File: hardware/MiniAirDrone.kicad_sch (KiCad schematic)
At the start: 15 parts, among them J1 USB_C_Receptacle_USB2.0, Q1 UMH3N, U1 CH340C, U2 ESP32-WROOM-32

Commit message: mpu6050
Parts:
- added C5: 0.1uF, symbol Device:C
- added C6: 2.2nF, symbol Device:C
- added R4, R? (x2): 10K, symbol Device:R
- added U3: MPU-6050, Sensor_Motion:InvenSense_QFN-24_4x4mm_P0.5mm, symbol Sensor_Motion:MPU-6050
- added U?: TS1117BCW33_RPG, Package_TO_SOT_SMD:SOT-223-3_TabPin2, symbol Regulator_Linear:TS1117BCW33_RPG
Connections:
- net +3.3V: now also R4.1, R?.1, R?.1, U3.13 (VDD), U3.8 (VDDIO), U?.2 (Output)
- net +5V: now also U?.3 (Input)
- net GND: now also C5.2, C6.2, U3.1 (CLKIN), U3.11 (FSYNC), U3.18 (GND), U3.9 (AD0), U?.1 (GND)
- new net: C5.1, U3.10 (REGOUT)
- new net: C6.1, U3.20 (CPOUT)
- new net AUX_SCL: R?.2, U3.7 (AUX_SCL)
- new net AUX_SDA: R?.2, U3.6 (AUX_SDA)
- new net IIC0_SCL: U3.23 (SCL)
- new net IIC0_SDA: U3.24 (SDA)
- new net MPU_INT: R4.2, U3.12 (INT)
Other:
- note added: "MPU6050"
- note added: "POWER"
- moved on the sheet: C1, C2, J1, Q1A, Q1B, R1, R2, R3, TP1, TP2, U1

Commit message: sth
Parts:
- removed R4, R? (x2): 10K, symbol Device:R
- added U?: MS5611-01BA, Package_LGA:LGA-8_3x5mm_P1.25mm, symbol Sensor_Pressure:MS5611-01BA
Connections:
- net +3.3V: now also U?.1 (VDD), U?.2 (PS)
- net GND: now also U?.3 (GND), U?.4 (CSB), U?.5 (CSB)
- net IIC0_SCL: now also U2.36 (IO22), U?.8 (SCLK)
- net IIC0_SDA: now also U?.7 (SDI/SDA)
- net AUX_SCL: no longer names the net of U3.7 (AUX_SCL)
- net AUX_SDA: no longer names the net of U3.6 (AUX_SDA)
- net MPU_INT: no longer names the net of U3.12 (INT)
- no-connect marks 7 -> 11
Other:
- note added: "IIC0_SDA"
- note added: "MS5611 气压计"

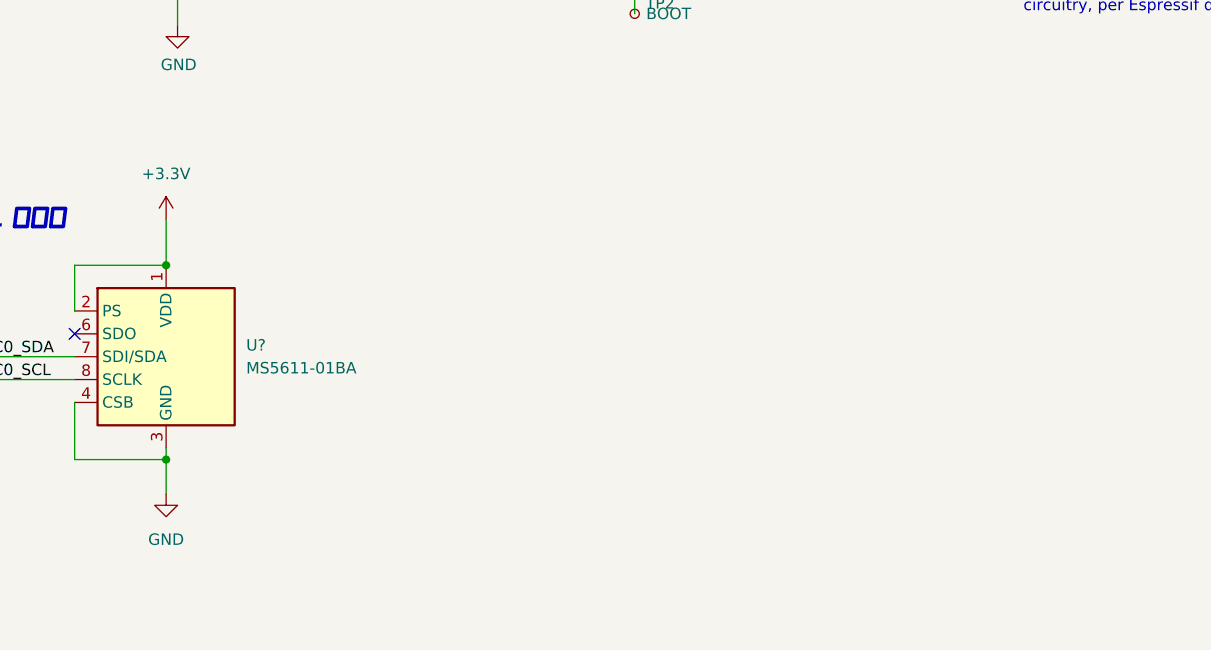
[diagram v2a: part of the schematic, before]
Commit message: Update MiniAirDrone.kicad_sch
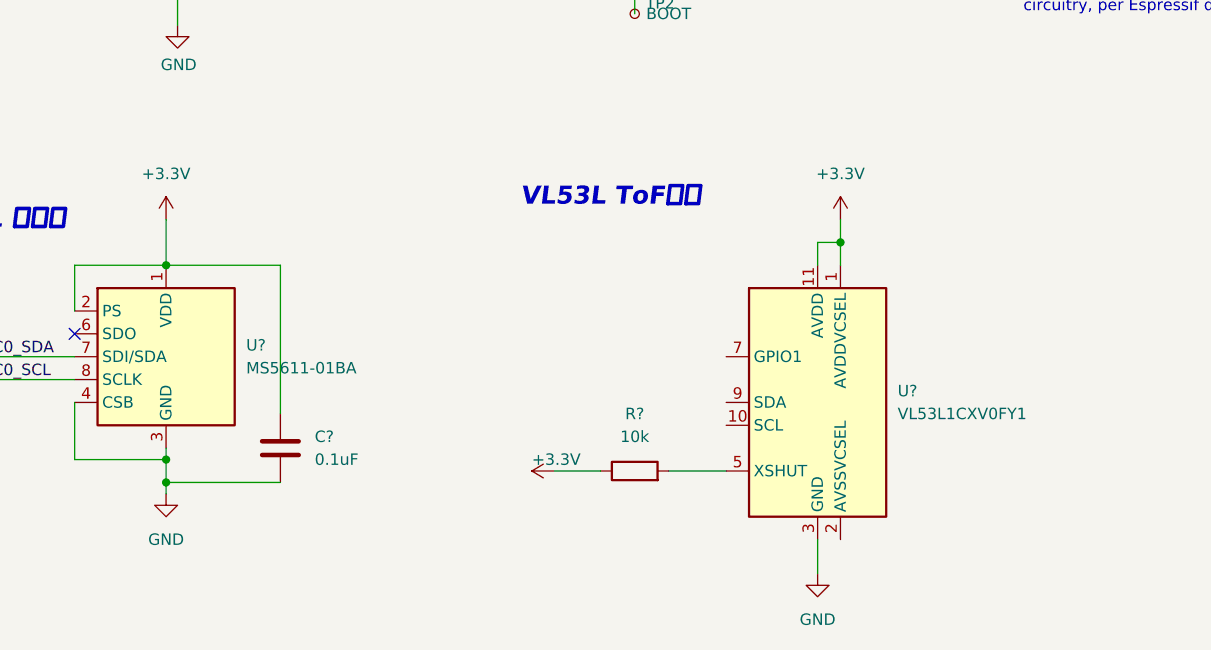
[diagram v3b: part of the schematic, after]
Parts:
- added C?: 0.1uF, symbol Device:C
- added R?: 10k, symbol Device:R
- added U?: VL53L1CXV0FY1, Sensor_Distance:ST_VL53L1x, symbol Sensor_Distance:VL53L1CXV0FY1
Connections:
- net +3.3V: now also C?.1, R?.1, U?.1 (AVDDVCSEL), U?.11 (AVDD)
- net GND: now also C?.2, U?.12 (GND), U?.3 (GND), U?.4 (GND), U?.6 (GND)
- new net: R?.2, U?.5 (XSHUT)
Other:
- note added: "VL53L ToF测距"
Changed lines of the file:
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@@
   (junction (at 191.77 38.1) (diameter 0) (color 0 0 0 0)
   )
+  (junction (at 191.77 88.9) (diameter 0) (color 0 0 0 0)
+  )
   (junction (at 34.29 67.31) (diameter 0) (color 0 0 0 0)
   )
@@
   )
   (junction (at 26.67 67.31) (diameter 0) (color 0 0 0 0)
+  )
+  (junction (at 116.84 115.57) (diameter 0) (color 0 0 0 0)
   )
   (junction (at 49.53 41.91) (diameter 0) (color 0 0 0 0)
@@
     (stroke (width 0) (type default) (color 0 0 0 0))
   )
+  (wire (pts (xy 189.23 121.92) (xy 189.23 125.73))
+    (stroke (width 0) (type default) (color 0 0 0 0))
+  )
   (wire (pts (xy 118.11 25.4) (xy 116.84 25.4))
     (stroke (width 0) (type default) (color 0 0 0 0))
@@
     (stroke (width 0) (type default) (color 0 0 0 0))
   )
+  (wire (pts (xy 189.23 91.44) (xy 189.23 88.9))
+    (stroke (width 0) (type default) (color 0 0 0 0))
+  )
+  (wire (pts (xy 160.02 114.3) (xy 165.1 114.3))
+    (stroke (width 0) (type default) (color 0 0 0 0))
+  )
   (wire (pts (xy 373.38 41.91) (xy 392.43 41.91))
     (stroke (width 0) (type default) (color 0 0 0 0))
@@
     (stroke (width 0) (type default) (color 0 0 0 0))
   )
-  (wire (pts (xy 116.84 113.03) (xy 116.84 116.84))
+  (wire (pts (xy 116.84 113.03) (xy 116.84 115.57))
     (stroke (width 0) (type default) (color 0 0 0 0))
   )
@@
     (stroke (width 0) (type default) (color 0 0 0 0))
   )
+  (wire (pts (xy 116.84 115.57) (xy 116.84 116.84))
+    (stroke (width 0) (type default) (color 0 0 0 0))
+  )
   (wire (pts (xy 35.56 116.84) (xy 30.48 116.84))
     (stroke (width 0) (type default) (color 0 0 0 0))
@@
     (stroke (width 0) (type default) (color 0 0 0 0))
   )
+  (wire (pts (xy 189.23 88.9) (xy 191.77 88.9))
+    (stroke (width 0) (type default) (color 0 0 0 0))
+  )
   (wire (pts (xy 74.93 125.73) (xy 74.93 127))
     (stroke (width 0) (type default) (color 0 0 0 0))
@@
     (stroke (width 0) (type default) (color 0 0 0 0))
   )
+  (wire (pts (xy 191.77 86.36) (xy 191.77 88.9))
+    (stroke (width 0) (type default) (color 0 0 0 0))
+  )
   (wire (pts (xy 19.05 101.6) (xy 35.56 101.6))
     (stroke (width 0) (type default) (color 0 0 0 0))
@@
     (stroke (width 0) (type default) (color 0 0 0 0))
   )
+  (wire (pts (xy 172.72 114.3) (xy 179.07 114.3))
+    (stroke (width 0) (type default) (color 0 0 0 0))
+  )
+  (wire (pts (xy 129.54 107.95) (xy 129.54 91.44))
+    (stroke (width 0) (type default) (color 0 0 0 0))
+  )
   (wire (pts (xy 19.05 104.14) (xy 35.56 104.14))
     (stroke (width 0) (type default) (color 0 0 0 0))
@@
     (stroke (width 0) (type default) (color 0 0 0 0))
   )
+  (wire (pts (xy 129.54 91.44) (xy 116.84 91.44))
+    (stroke (width 0) (type default) (color 0 0 0 0))
+  )
   (wire (pts (xy 53.34 29.21) (xy 63.5 29.21))
     (stroke (width 0) (type default) (color 0 0 0 0))
@@
     (stroke (width 0) (type default) (color 0 0 0 0))
   )
+  (wire (pts (xy 129.54 115.57) (xy 116.84 115.57))
+    (stroke (width 0) (type default) (color 0 0 0 0))
+  )
   (wire (pts (xy 325.12 30.48) (xy 325.12 33.02))
     (stroke (width 0) (type default) (color 0 0 0 0))
@@
   )
   (wire (pts (xy 50.8 86.36) (xy 50.8 91.44))
+    (stroke (width 0) (type default) (color 0 0 0 0))
+  )
+  (wire (pts (xy 191.77 88.9) (xy 191.77 91.44))
     (stroke (width 0) (type default) (color 0 0 0 0))
   )
@@
   )
   (text "MPU6050" (at 19.05 88.9 0)
+    (effects (font (size 2.0066 2.0066) (thickness 0.4013) bold italic) (justify left bottom))
+  )
+  (text "VL53L ToF测距" (at 156.21 85.09 0)
     (effects (font (size 2.0066 2.0066) (thickness 0.4013) bold italic) (justify left bottom))
   )
@@
     (pin "1")
   )
+  (symbol (lib_id "Device:C") (at 129.54 111.76 0) (unit 1)
+    (in_bom yes) (on_board yes) (fields_autoplaced)
+    (property "Reference" "C?" (id 0) (at 133.35 110.4899 0)
+      (effects (font (size 1.27 1.27)) (justify left))
+    )
+    (property "Value" "0.1uF" (id 1) (at 133.35 113.0299 0)
+      (effects (font (size 1.27 1.27)) (justify left))
+    )
+    (property "Footprint" "" (id 2) (at 130.5052 115.57 0)
+      (effects (font (size 1.27 1.27)) hide)
+    )
+    (property "Datasheet" "~" (id 3) (at 129.54 111.76 0)
+      (effects (font (size 1.27 1.27)) hide)
+    )
+    (pin "1")
+    (pin "2")
+  )
   (symbol (lib_id "power:GND") (at 325.12 33.02 0) (unit 1)
     (in_bom yes) (on_board yes)
@@
     )
     (property "Datasheet" "" (id 3) (at 325.12 33.02 0)
+      (effects (font (size 1.27 1.27)) hide)
+    )
+    (pin "1")
+  )
+  (symbol (lib_id "power:GND") (at 189.23 125.73 0) (unit 1)
+    (in_bom yes) (on_board yes) (fields_autoplaced)
+    (property "Reference" "#PWR?" (id 0) (at 189.23 132.08 0)
+      (effects (font (size 1.27 1.27)) hide)
+    )
+    (property "Value" "GND" (id 1) (at 189.23 130.81 0))
+    (property "Footprint" "" (id 2) (at 189.23 125.73 0)
+      (effects (font (size 1.27 1.27)) hide)
+    )
+    (property "Datasheet" "" (id 3) (at 189.23 125.73 0)
       (effects (font (size 1.27 1.27)) hide)
     )
@@
     (pin "1")
   )
+  (symbol (lib_id "Sensor_Distance:VL53L1CXV0FY1") (at 189.23 106.68 0) (unit 1)
+    (in_bom yes) (on_board yes) (fields_autoplaced)
+    (property "Reference" "U?" (id 0) (at 198.12 105.4099 0)
+      (effects (font (size 1.27 1.27)) (justify left))
+    )
+    (property "Value" "VL53L1CXV0FY1" (id 1) (at 198.12 107.9499 0)
+      (effects (font (size 1.27 1.27)) (justify left))
+    )
+    (property "Footprint" "Sensor_Distance:ST_VL53L1x" (id 2) (at 206.375 120.65 0)
+      (effects (font (size 1.27 1.27)) hide)
+    )
+    (property "Datasheet" "https://www.st.com/resource/en/datasheet/vl53l1x.pdf" (id 3) (at 191.77 106.68 0)
+      (effects (font (size 1.27 1.27)) hide)
+    )
+    (pin "1")
+    (pin "10")
+    (pin "11")
+    (pin "12")
+    (pin "2")
+    (pin "3")
+    (pin "4")
+    (pin "5")
+    (pin "6")
+    (pin "7")
+    (pin "8")
+    (pin "9")
+  )
   (symbol (lib_id "Connector:USB_C_Receptacle_USB2.0") (at 34.29 44.45 0) (unit 1)
     (in_bom yes) (on_board yes)
@@
     (pin "1")
   )
+  (symbol (lib_id "power:+3.3V") (at 191.77 86.36 0) (unit 1)
+    (in_bom yes) (on_board yes) (fields_autoplaced)
+    (property "Reference" "#PWR?" (id 0) (at 191.77 90.17 0)
+      (effects (font (size 1.27 1.27)) hide)
+    )
+    (property "Value" "+3.3V" (id 1) (at 191.77 81.28 0))
+    (property "Footprint" "" (id 2) (at 191.77 86.36 0)
+      (effects (font (size 1.27 1.27)) hide)
+    )
+    (property "Datasheet" "" (id 3) (at 191.77 86.36 0)
+      (effects (font (size 1.27 1.27)) hide)
+    )
+    (pin "1")
+  )
   (symbol (lib_id "Device:C_Small") (at 101.6 27.94 0) (unit 1)
     (in_bom yes) (on_board yes)
@@
     (pin "3")
   )
+  (symbol (lib_id "power:+3.3V") (at 160.02 114.3 90) (unit 1)
+    (in_bom yes) (on_board yes)
+    (property "Reference" "#PWR?" (id 0) (at 163.83 114.3 0)
+      (effects (font (size 1.27 1.27)) hide)
+    )
+    (property "Value" "+3.3V" (id 1) (at 157.48 113.03 90)
+      (effects (font (size 1.27 1.27)) (justify right))
+    )
+    (property "Footprint" "" (id 2) (at 160.02 114.3 0)
+      (effects (font (size 1.27 1.27)) hide)
+    )
+    (property "Datasheet" "" (id 3) (at 160.02 114.3 0)
+      (effects (font (size 1.27 1.27)) hide)
+    )
+    (pin "1")
+  )
+  (symbol (lib_id "Device:R") (at 168.91 114.3 90) (unit 1)
+    (in_bom yes) (on_board yes) (fields_autoplaced)
+    (property "Reference" "R?" (id 0) (at 168.91 107.95 90))
+    (property "Value" "10k" (id 1) (at 168.91 110.49 90))
+    (property "Footprint" "" (id 2) (at 168.91 116.078 90)
+      (effects (font (size 1.27 1.27)) hide)
+    )
+    (property "Datasheet" "~" (id 3) (at 168.91 114.3 0)
+      (effects (font (size 1.27 1.27)) hide)
+    )
+    (pin "1")
+    (pin "2")
+  )
   (symbol (lib_id "power:GND") (at 116.84 116.84 0) (unit 1)
     (in_bom yes) (on_board yes) (fields_autoplaced)
@@
       (reference "#PWR0104") (unit 1) (value "+3.3V") (footprint "")
     )
+    (path "/148a5e03-072c-4484-9e51-37470a88c59e"
+      (reference "#PWR?") (unit 1) (value "GND") (footprint "")
+    )
     (path "/a1df0c77-697f-4aaa-8640-bc336235aa7b"
       (reference "#PWR?") (unit 1) (value "GND") (footprint "")
@@
       (reference "#PWR?") (unit 1) (value "+5V") (footprint "")
     )
+    (path "/d64b865b-9122-4cad-a4be-318d2b26ed77"
+      (reference "#PWR?") (unit 1) (value "+3.3V") (footprint "")
+    )
+    (path "/e7327349-aefb-4985-9b20-ceccbdee223c"
+      (reference "#PWR?") (unit 1) (value "+3.3V") (footprint "")
+    )
     (path "/ed5cddfb-1f56-4027-8f78-d3b9de36bf24"
       (reference "#PWR?") (unit 1) (value "GND") (footprint "")
@@
       (reference "C6") (unit 1) (value "2.2nF") (footprint "")
     )
+    (path "/090db0b3-d833-4c83-8505-e9354bf840a5"
+      (reference "C?") (unit 1) (value "0.1uF") (footprint "")
+    )
     (path "/b74a2c11-24dd-463c-aa73-ee48758aca8f"
       (reference "J1") (unit 1) (value "USB_C_Receptacle_USB2.0") (footprint "GCT_USB:USB4510_NoPaste")
@@
       (reference "R3") (unit 1) (value "10k") (footprint "Resistor_SMD:R_0603_1608Metric")
     )
+    (path "/e880ff73-bb9a-4b1a-8d91-0e076997b870"
+      (reference "R?") (unit 1) (value "10k") (footprint "")
+    )
     (path "/98ba0a2d-5220-459d-85c7-f69c1fdb0d6f"
       (reference "TP1") (unit 1) (value "EN") (footprint "Modified:TestPoint_Pad_D2.0mm_ValueSilk")
@@
       (reference "U?") (unit 1) (value "MS5611-01BA") (footprint "Package_LGA:LGA-8_3x5mm_P1.25mm")
     )
+    (path "/b605366b-478c-481d-b6eb-1a3e084f5c67"
+      (reference "U?") (unit 1) (value "VL53L1CXV0FY1") (footprint "Sensor_Distance:ST_VL53L1x")
+    )
     (path "/e10a3c5d-cd59-4232-8dcc-fdf71667fa24"

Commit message: something
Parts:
- added R? (x2): 4.7k, symbol Device:R
- added R?: 10k, symbol Device:R
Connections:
- net +3.3V: now also R?.1, R?.1, R?.1
- net GND: now also U?.2 (AVSSVCSEL)
- net IIC0_SCL: now also U?.10 (SCL), R?.2
- net IIC0_SDA: now also U2.33 (IO21), U?.9 (SDA), R?.2
- net at U?.7 (GPIO1): now also R?.2
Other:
- note added: "PULL UP & DOWN"
- note removed: "IIC0_SDA"

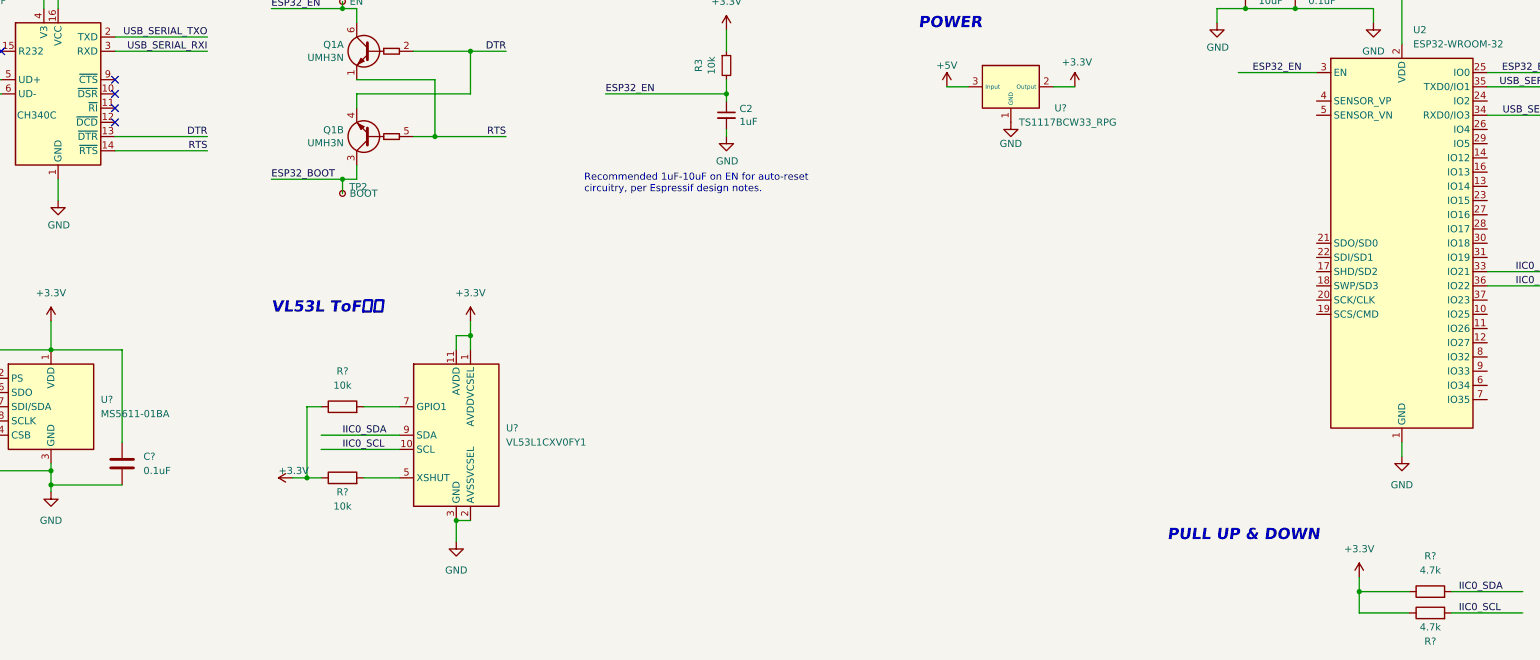
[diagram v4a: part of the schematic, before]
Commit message: Update MiniAirDrone.kicad_sch
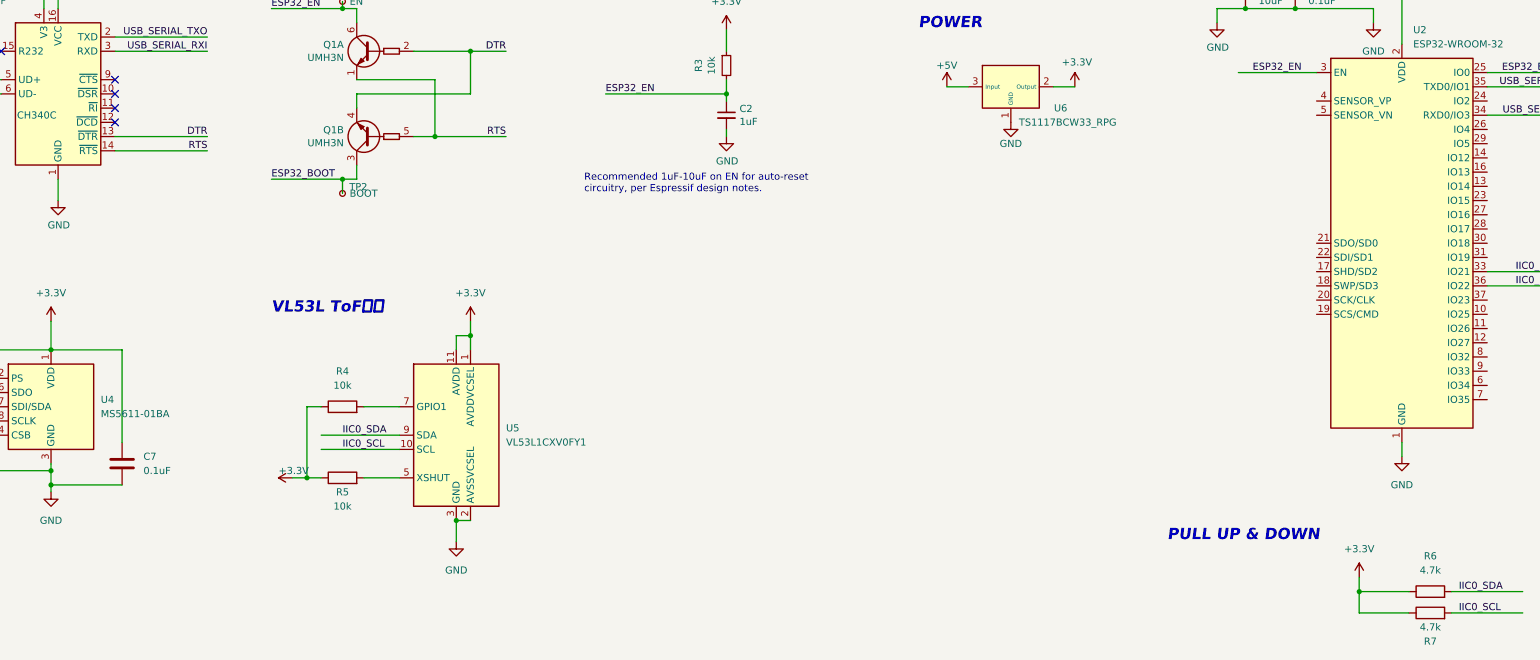
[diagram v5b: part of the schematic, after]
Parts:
- gave numbers to parts that had none: 8
